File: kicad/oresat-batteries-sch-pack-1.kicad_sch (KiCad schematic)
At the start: 79 parts, among them Q12 SI7625DN-T1-GE3, Q13 SI7625DN-T1-GE3, Q14 NTR4101, Q15 NTR4101, Q16 SI7625DN-T1-GE3, Q17 SI7625DN-T1-GE3, Q18 SI7625DN-T1-GE3, Q19 SI7625DN-T1-GE3, Q6 PM45VEN, Q7 PM45VEN, Q8 PM45VEN, Q9 PM45VEN, U10 LTC4412, U11 LTC4412, U12 MAX17205G, U8 S-8209AAA-T8T1U, U9 S-8209AAA-T8T1U

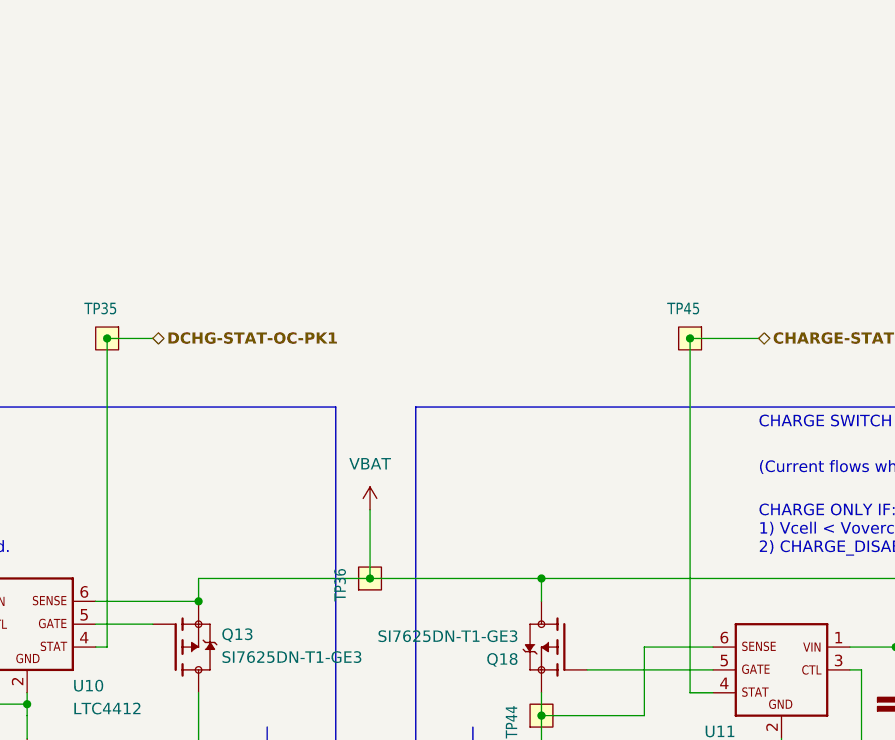
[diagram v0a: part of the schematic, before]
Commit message: Added +battery disconect mosfet and switch
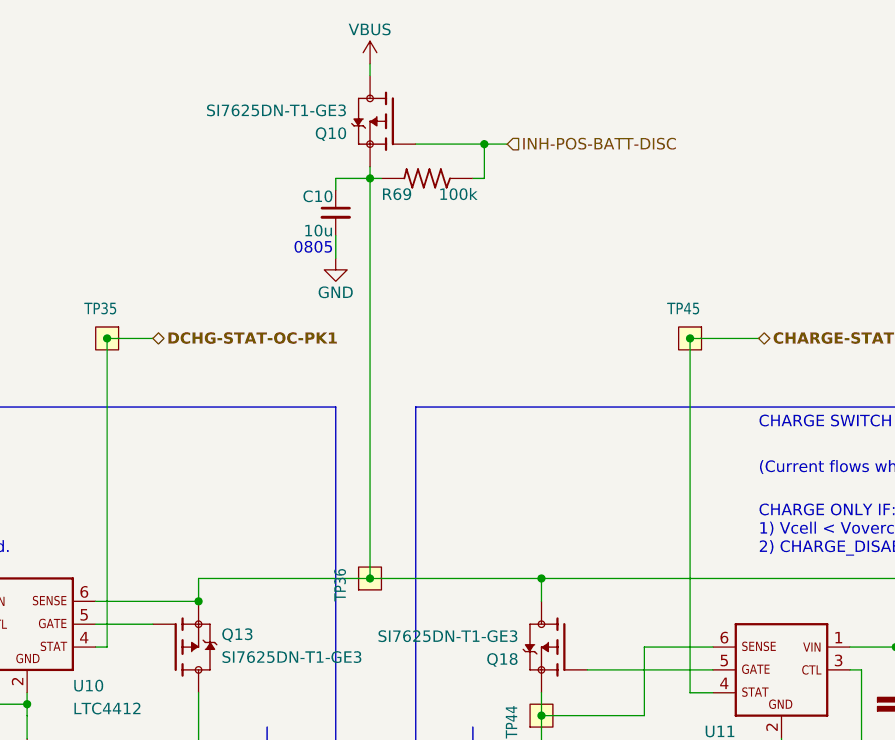
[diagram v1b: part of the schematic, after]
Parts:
- added C10: 10u, oresat-batteries:.0805-B-NOSILK, symbol Device:C_Small
- added Q10: SI7625DN-T1-GE3, oresat-batteries:POWERPAK-1212-8, symbol oresat-batteries-eagle-import:Q-VISHAY-MOSFET-PCH-POWERPAK-1212-8
- added R69: 100k, oresat-batteries:.0603-C-NOSILK, symbol oresat-batteries-eagle-import:R-US_0603-C-NOSILK
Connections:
- net GND: now also C10.2
- net VBAT: no longer names the net of C23.1, Q13.1 (S), Q13.2 (S), Q13.3 (S), Q18.5 (D), Q18.6 (D), Q18.7 (D), Q18.8 (D), Q18.PAD (D), TP36.1, U10.6 (SENSE), U11.1 (VIN)
- net VBAT: now also C10.1, Q10.1 (S), Q10.2 (S), Q10.3 (S), R69.2
- new net INH-POS-BATT-DISC: Q10.4 (G), R69.1
- new net VBUS: Q10.5 (D), Q10.6 (D), Q10.7 (D), Q10.8 (D), Q10.PAD (D)
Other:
- note added: "0805"

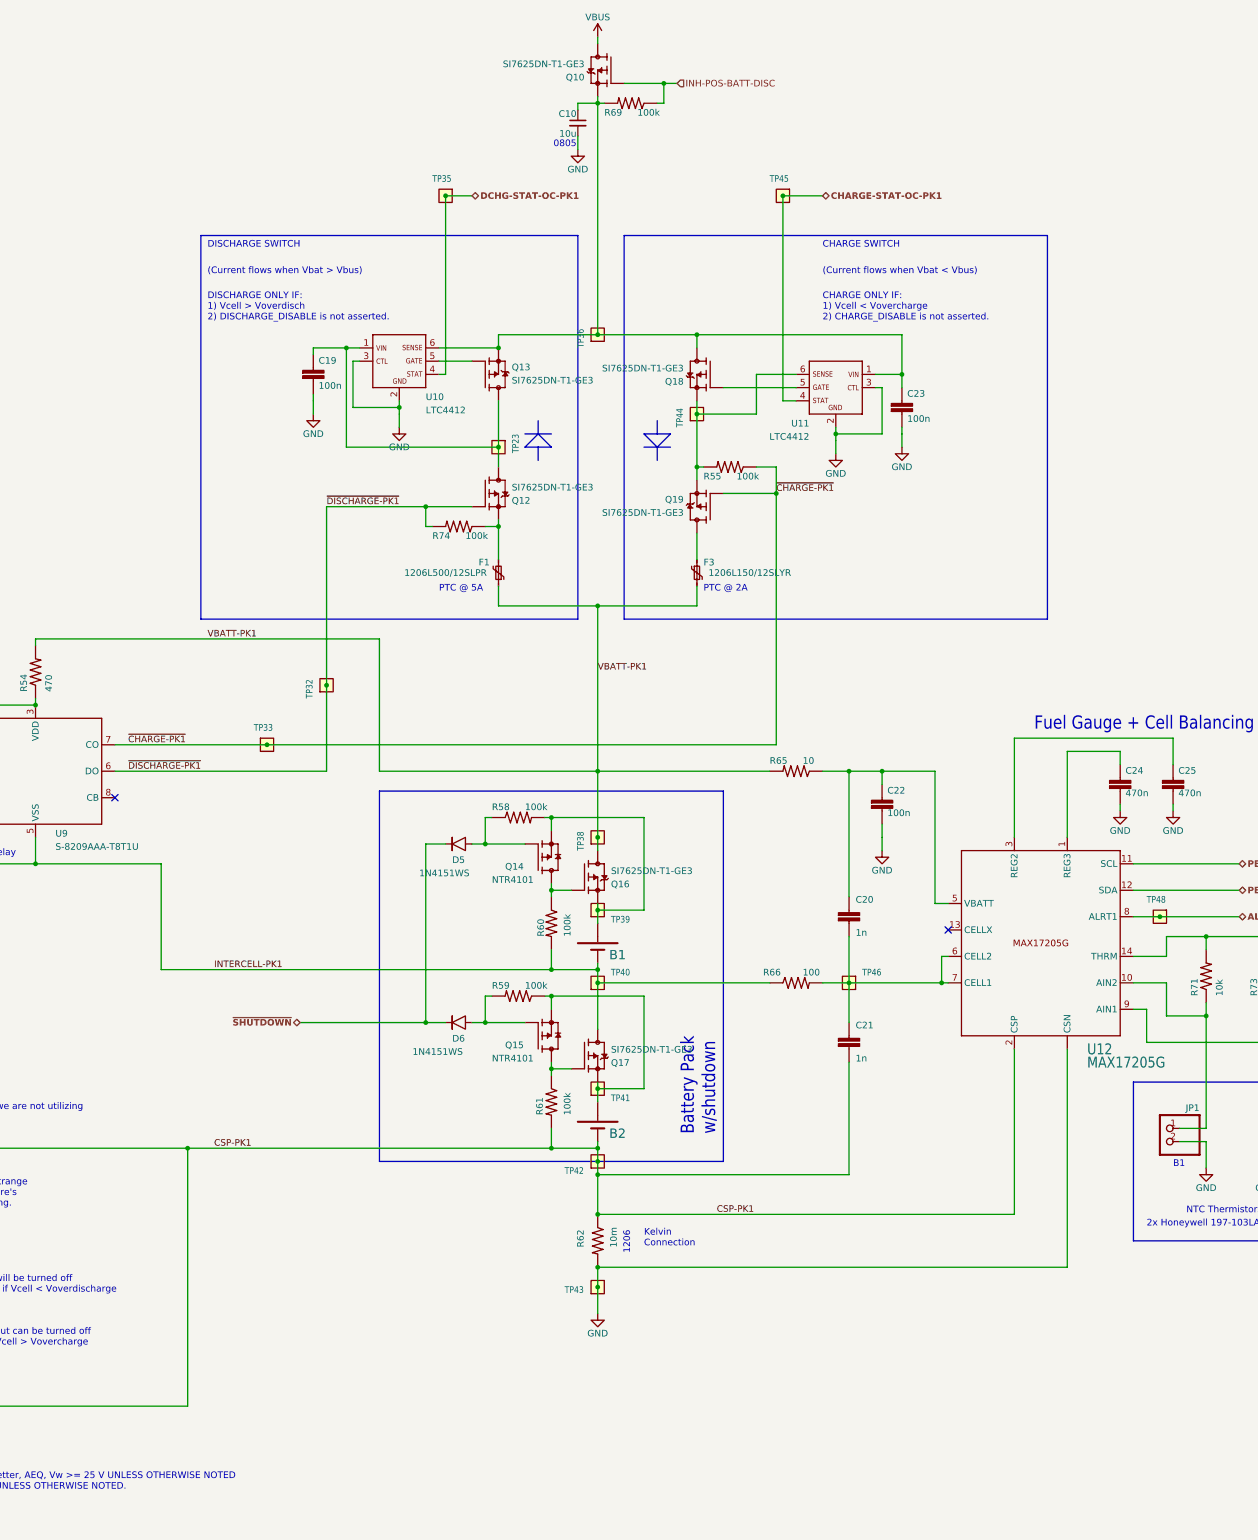
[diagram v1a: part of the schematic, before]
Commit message: Negative battery disconnects in. Ready for KiCad component upgrade.
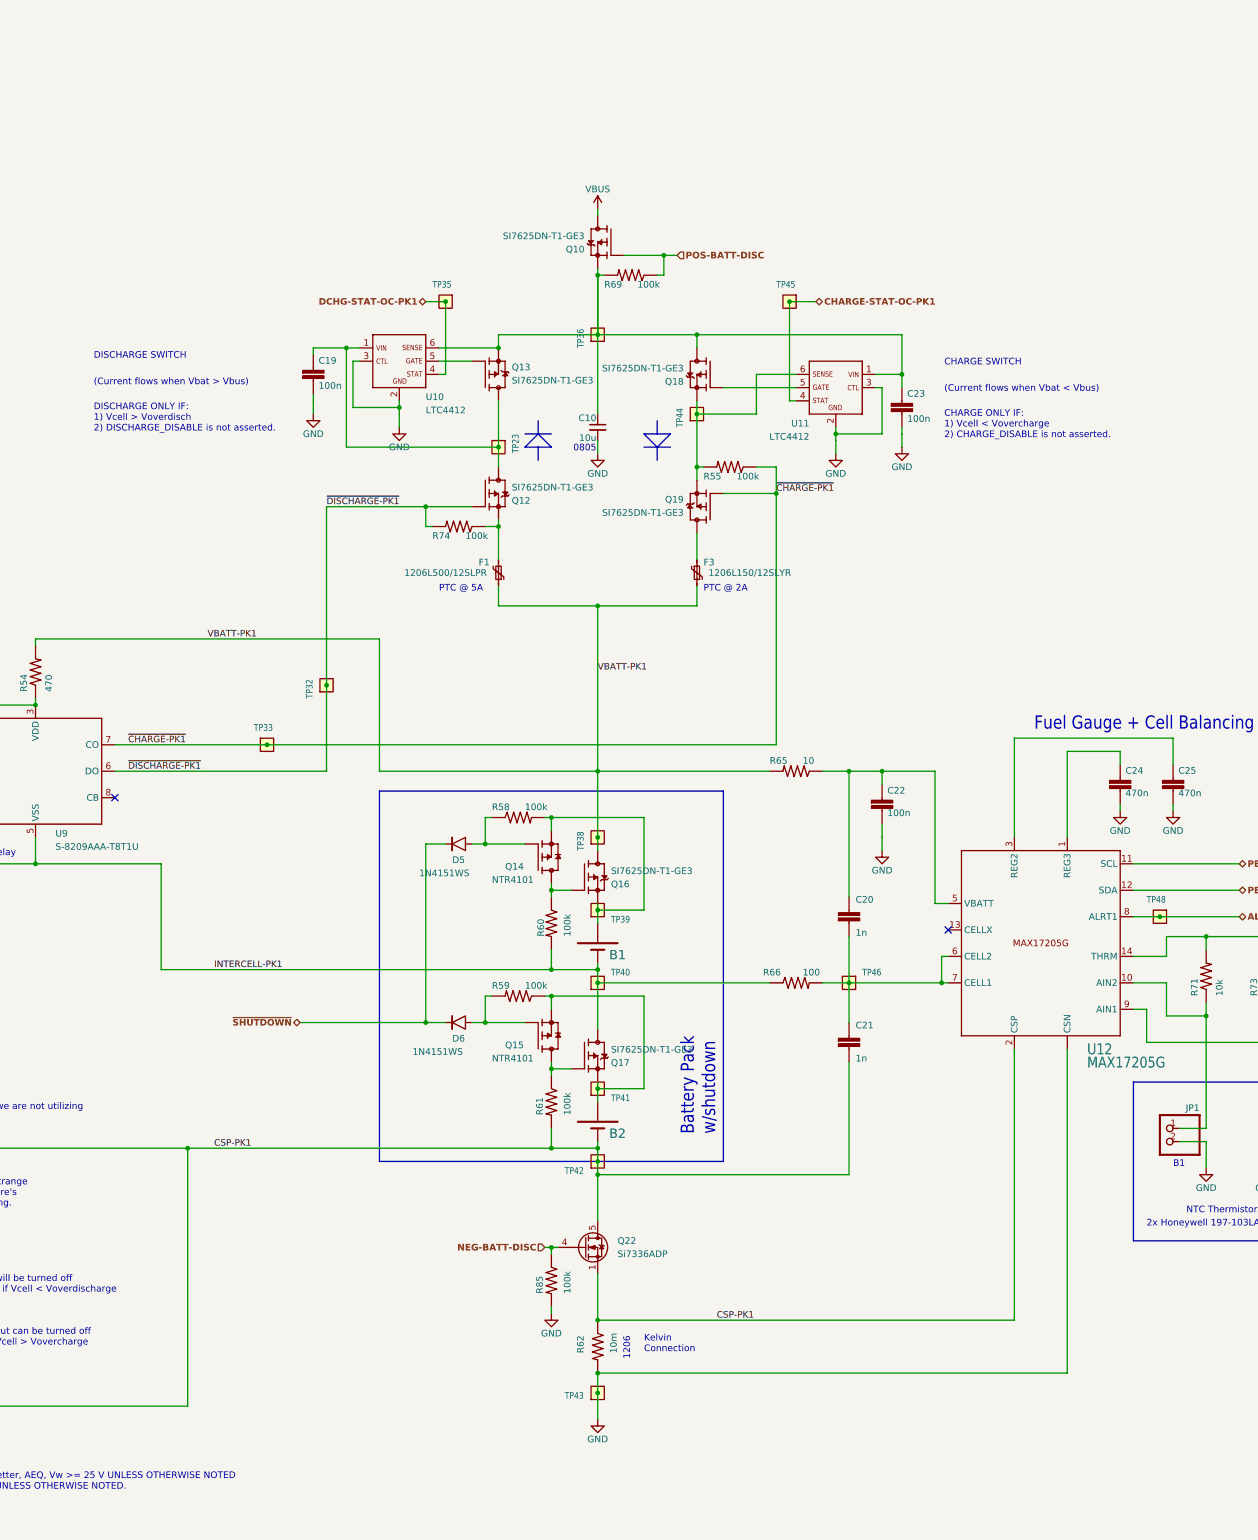
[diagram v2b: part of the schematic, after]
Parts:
- added Q22: Si7336ADP, Package_SO:PowerPAK_SO-8_Single, symbol Transistor_FET:Si7336ADP
- added R85: 100k, oresat-batteries:.0603-C-NOSILK, symbol oresat-batteries-eagle-import:R-US_0603-C-NOSILK
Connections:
- net CSP-PK1: now also Q22.1 (S), Q22.2 (S), Q22.3 (S), Q22.5 (D)
- net GND: now also R85.2
- net INH-POS-BATT-DISC renamed POS-BATT-DISC
- new net NEG-BATT-DISC: Q22.4 (G), R85.1
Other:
- moved on the sheet: C10, Q10, R62, R69, TP35, TP43, TP45

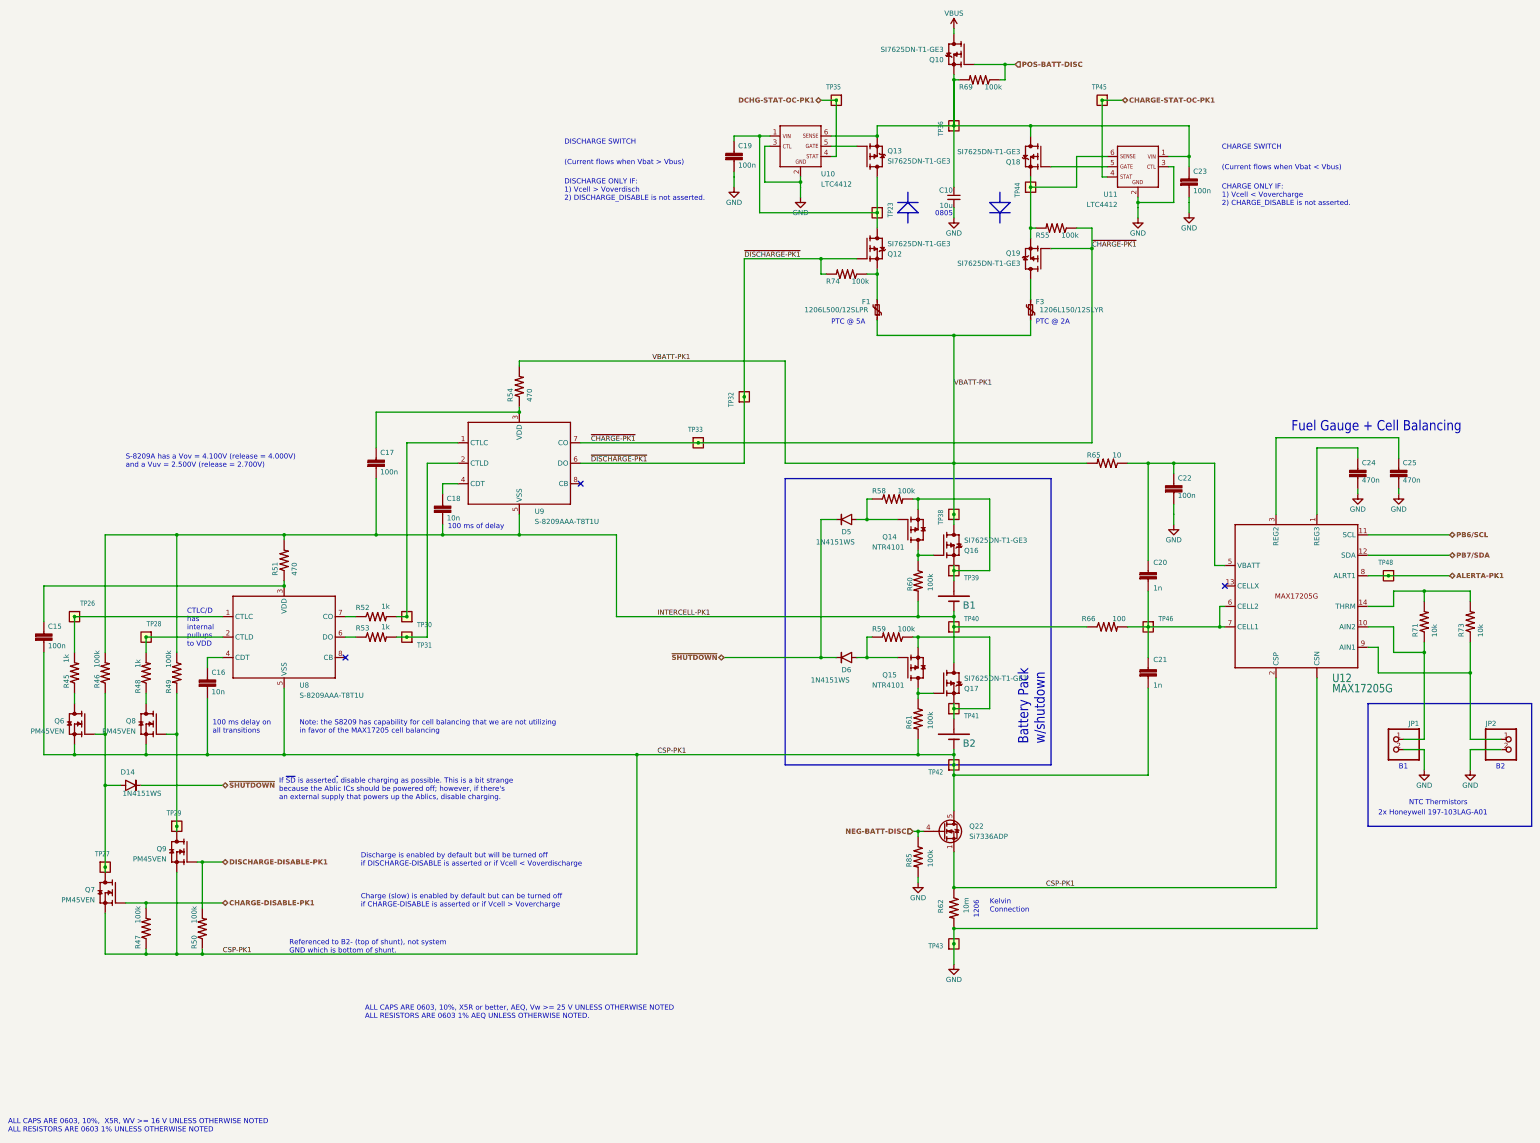
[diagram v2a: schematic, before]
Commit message: Renovated Schematic
Updated schematic symbols and made more uniform with changed resistor, capacitor, and FET symbols. Changed 0603 cap foot print to 0603 small in Oresat passives. Added 2 new resistors and 2 new caps in the power page. Removed old debug connector in favor of the new one. The changes made should make very little updates when pushing the changes to the PCB.
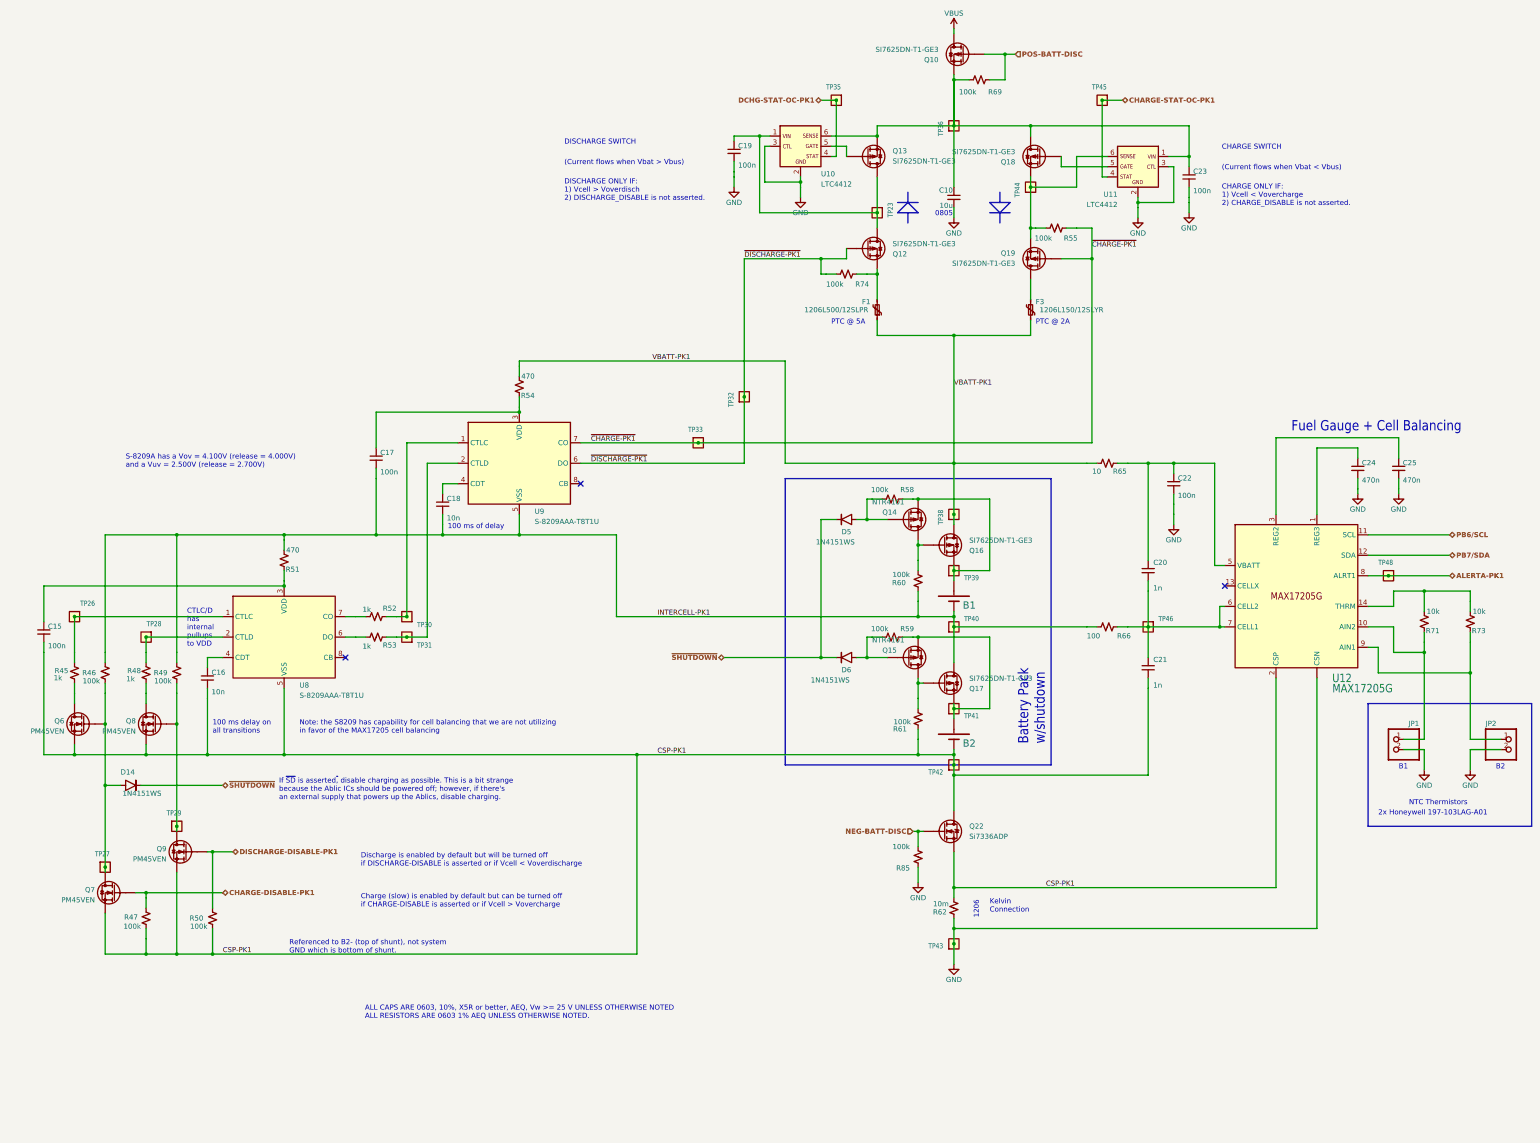
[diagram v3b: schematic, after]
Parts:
- C15, C16, C17, C18, C19, C20, C21, C22, C23, C24, C25: footprint oresat-batteries:.0603-C-NOSILK -> oresat-passives:c_0603-SMALL; symbol oresat-batteries-eagle-import:C-EU0603-C-NOSILK -> Device:C_Small
- Q14, Q15: symbol oresat-batteries-eagle-import:P-MOSFET-SOT23-3 -> Transistor_FET:Q_PMOS_GSD
- Q6, Q7, Q8, Q9: symbol oresat-batteries-eagle-import:N-MOSFET-SOT-23-3 -> Transistor_FET:Q_NMOS_GSD
- R45, R46, R47, R48, R49, R50, R51, R52, R53, R54, R55, R58, R59, R60, R61, R65, R66, R69, R71, R73, R74, R85: symbol oresat-batteries-eagle-import:R-US_0603-C-NOSILK -> Device:R_Small_US
- R62: symbol oresat-batteries-eagle-import:R-US_1206-C -> Device:R_Small_US
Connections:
- net INTERCELL-PK1: no longer Q17.6 (D), Q17.7 (D), Q17.8 (D), Q17.PAD (D)
- net VBATT-PK1: no longer Q16.6 (D), Q16.7 (D), Q16.8 (D), Q16.PAD (D)
- net VBUS: no longer Q10.6 (D), Q10.7 (D), Q10.8 (D), Q10.PAD (D)
- net at C10.1, C23.1, Q10.1 (S)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: no longer Q10.2 (S), Q10.3 (S), Q13.2 (S), Q13.3 (S), Q18.6 (D), Q18.7 (D), Q18.8 (D), Q18.PAD (D)
- net at B2.1 (POS), Q15.2 (S), Q17.1 (S)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: no longer Q17.2 (S), Q17.3 (S)
- net at B1.1 (POS), Q14.2 (S), Q16.1 (S)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: no longer Q16.2 (S), Q16.3 (S)
- net at Q18.1 (S), Q19.1 (S), R55.2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: no longer Q18.2 (S), Q18.3 (S), Q19.2 (S), Q19.3 (S)
- net at F1.2, Q12.1 (S), R74.1: no longer Q12.2 (S), Q12.3 (S)
- new net: C19.1, Q12.5 (D), Q13.5 (D), TP23.1, U10.1 (VIN)
- new net: F3.1, Q19.5 (D)
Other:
- note removed: "ALL CAPS ARE 0603, 10%, X5R, WV >= 16 V UNLESS OTHERWISE NOTED ALL RESISTORS ARE 0603 1% UNLESS OTHERWISE NOTED"
